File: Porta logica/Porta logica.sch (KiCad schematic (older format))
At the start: 60 parts, among them P1 Input, P2 Batteria, P3 Out, SW1 SW_PUSH, SW2 SW_PUSH, U1 74HC595, U2 LM7805, U3 74HC595, U4 74HC00, U5 74HC595

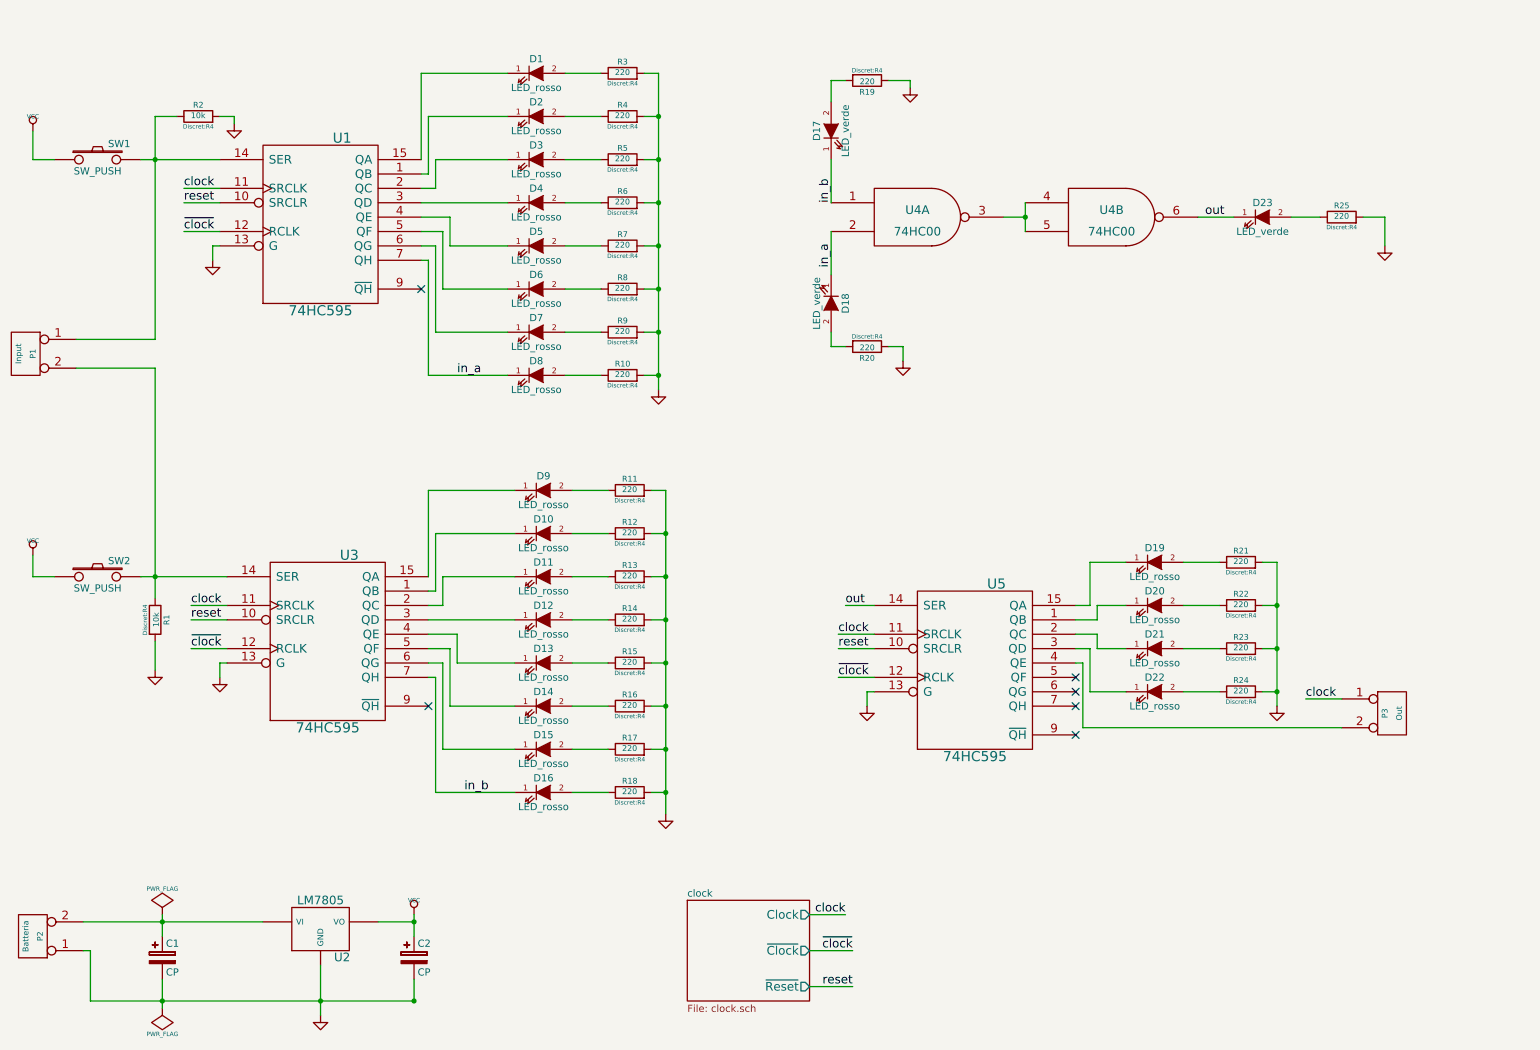
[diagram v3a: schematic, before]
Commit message: Aggiorna footprint resistenze
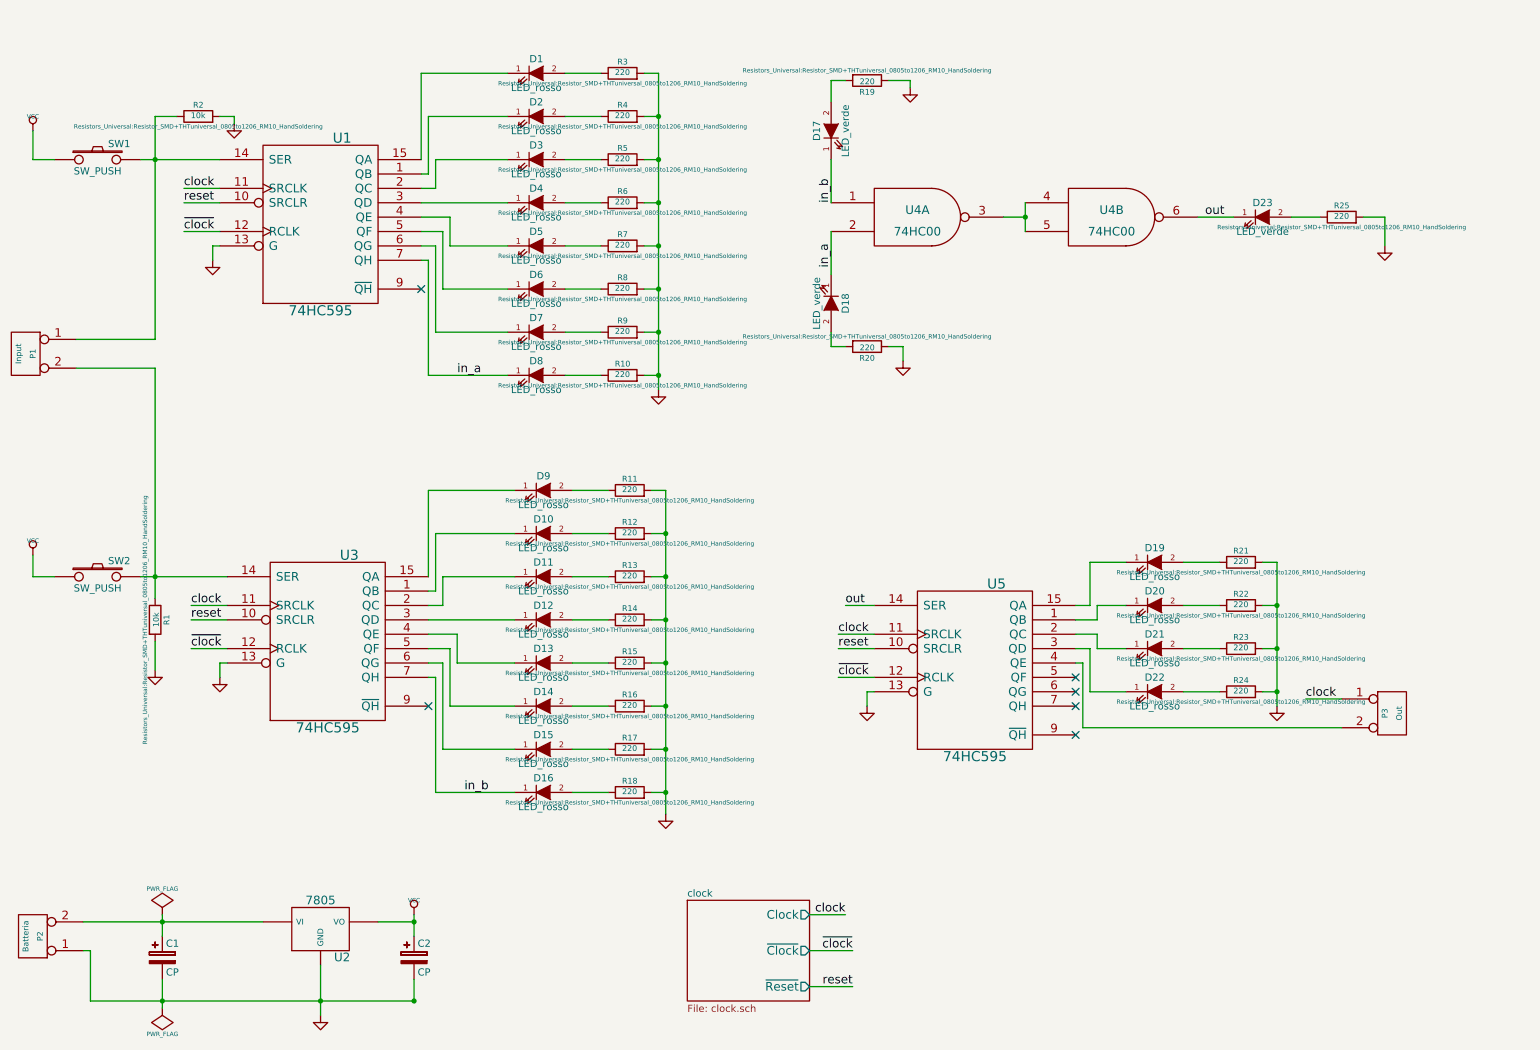
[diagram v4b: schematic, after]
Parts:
- removed U2: LM7805, Housings_SOIC:SOIC-16_7.5x10.3mm_Pitch1.27mm, symbol LM7805
- added U2: 7805, Housings_SOIC:SOIC-16_7.5x10.3mm_Pitch1.27mm, symbol 7805
- R1, R10, R11, R12, R13, R14, R15, R16, R17, R18, R19, R2, R20, R21, R22, R23, R24, R25, R3, R4, R5, R6, R7, R8, R9: footprint Discret:R4 -> Resistors_Universal:Resistor_SMD+THTuniversal_0805to1206_RM10_HandSoldering
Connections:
- net GND: now also U2.GND
- net VCC: now also U2.VO
- net at C1.1, P2.2 (PM): now also U2.VI
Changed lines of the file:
@@
 F 0 "R3" V 4930 1000 40  0000 C CNN
 F 1 "220" V 4857 1001 40  0000 C CNN
-F 2 "Discret:R4" V 4780 1000 30  0000 C CNN
+F 2 "Resistors_Universal:Resistor_SMD+THTuniversal_0805to1206_RM10_HandSoldering" V 4780 1000 30  0000 C CNN
 F 3 "~" H 4850 1000 30  0000 C CNN
 	1    4850 1000
@@
 F 0 "R4" V 4930 1300 40  0000 C CNN
 F 1 "220" V 4857 1301 40  0000 C CNN
-F 2 "Discret:R4" V 4780 1300 30  0000 C CNN
+F 2 "Resistors_Universal:Resistor_SMD+THTuniversal_0805to1206_RM10_HandSoldering" V 4780 1300 30  0000 C CNN
 F 3 "~" H 4850 1300 30  0000 C CNN
 	1    4850 1300
@@
 F 0 "R5" V 4930 1600 40  0000 C CNN
 F 1 "220" V 4857 1601 40  0000 C CNN
-F 2 "Discret:R4" V 4780 1600 30  0000 C CNN
+F 2 "Resistors_Universal:Resistor_SMD+THTuniversal_0805to1206_RM10_HandSoldering" V 4780 1600 30  0000 C CNN
 F 3 "~" H 4850 1600 30  0000 C CNN
 	1    4850 1600
@@
 F 0 "R6" V 4930 1900 40  0000 C CNN
 F 1 "220" V 4857 1901 40  0000 C CNN
-F 2 "Discret:R4" V 4780 1900 30  0000 C CNN
+F 2 "Resistors_Universal:Resistor_SMD+THTuniversal_0805to1206_RM10_HandSoldering" V 4780 1900 30  0000 C CNN
 F 3 "~" H 4850 1900 30  0000 C CNN
 	1    4850 1900
@@
 F 0 "R7" V 4930 2200 40  0000 C CNN
 F 1 "220" V 4857 2201 40  0000 C CNN
-F 2 "Discret:R4" V 4780 2200 30  0000 C CNN
+F 2 "Resistors_Universal:Resistor_SMD+THTuniversal_0805to1206_RM10_HandSoldering" V 4780 2200 30  0000 C CNN
 F 3 "~" H 4850 2200 30  0000 C CNN
 	1    4850 2200
@@
 F 0 "R8" V 4930 2500 40  0000 C CNN
 F 1 "220" V 4857 2501 40  0000 C CNN
-F 2 "Discret:R4" V 4780 2500 30  0000 C CNN
+F 2 "Resistors_Universal:Resistor_SMD+THTuniversal_0805to1206_RM10_HandSoldering" V 4780 2500 30  0000 C CNN
 F 3 "~" H 4850 2500 30  0000 C CNN
 	1    4850 2500
@@
 F 0 "R9" V 4930 2800 40  0000 C CNN
 F 1 "220" V 4857 2801 40  0000 C CNN
-F 2 "Discret:R4" V 4780 2800 30  0000 C CNN
+F 2 "Resistors_Universal:Resistor_SMD+THTuniversal_0805to1206_RM10_HandSoldering" V 4780 2800 30  0000 C CNN
 F 3 "~" H 4850 2800 30  0000 C CNN
 	1    4850 2800
@@
 F 0 "R10" V 4930 3100 40  0000 C CNN
 F 1 "220" V 4857 3101 40  0000 C CNN
-F 2 "Discret:R4" V 4780 3100 30  0000 C CNN
+F 2 "Resistors_Universal:Resistor_SMD+THTuniversal_0805to1206_RM10_HandSoldering" V 4780 3100 30  0000 C CNN
 F 3 "~" H 4850 3100 30  0000 C CNN
 	1    4850 3100
@@
 F 0 "R11" V 4980 3900 40  0000 C CNN
 F 1 "220" V 4907 3901 40  0000 C CNN
-F 2 "Discret:R4" V 4830 3900 30  0000 C CNN
+F 2 "Resistors_Universal:Resistor_SMD+THTuniversal_0805to1206_RM10_HandSoldering" V 4830 3900 30  0000 C CNN
 F 3 "~" H 4900 3900 30  0000 C CNN
 	1    4900 3900
@@
 F 0 "R12" V 4980 4200 40  0000 C CNN
 F 1 "220" V 4907 4201 40  0000 C CNN
-F 2 "Discret:R4" V 4830 4200 30  0000 C CNN
+F 2 "Resistors_Universal:Resistor_SMD+THTuniversal_0805to1206_RM10_HandSoldering" V 4830 4200 30  0000 C CNN
 F 3 "~" H 4900 4200 30  0000 C CNN
 	1    4900 4200
@@
 F 0 "R13" V 4980 4500 40  0000 C CNN
 F 1 "220" V 4907 4501 40  0000 C CNN
-F 2 "Discret:R4" V 4830 4500 30  0000 C CNN
+F 2 "Resistors_Universal:Resistor_SMD+THTuniversal_0805to1206_RM10_HandSoldering" V 4830 4500 30  0000 C CNN
 F 3 "~" H 4900 4500 30  0000 C CNN
 	1    4900 4500
@@
 F 0 "R14" V 4980 4800 40  0000 C CNN
 F 1 "220" V 4907 4801 40  0000 C CNN
-F 2 "Discret:R4" V 4830 4800 30  0000 C CNN
+F 2 "Resistors_Universal:Resistor_SMD+THTuniversal_0805to1206_RM10_HandSoldering" V 4830 4800 30  0000 C CNN
 F 3 "~" H 4900 4800 30  0000 C CNN
 	1    4900 4800
@@
 F 0 "R15" V 4980 5100 40  0000 C CNN
 F 1 "220" V 4907 5101 40  0000 C CNN
-F 2 "Discret:R4" V 4830 5100 30  0000 C CNN
+F 2 "Resistors_Universal:Resistor_SMD+THTuniversal_0805to1206_RM10_HandSoldering" V 4830 5100 30  0000 C CNN
 F 3 "~" H 4900 5100 30  0000 C CNN
 	1    4900 5100
@@
 F 0 "R16" V 4980 5400 40  0000 C CNN
 F 1 "220" V 4907 5401 40  0000 C CNN
-F 2 "Discret:R4" V 4830 5400 30  0000 C CNN
+F 2 "Resistors_Universal:Resistor_SMD+THTuniversal_0805to1206_RM10_HandSoldering" V 4830 5400 30  0000 C CNN
 F 3 "~" H 4900 5400 30  0000 C CNN
 	1    4900 5400
@@
 F 0 "R17" V 4980 5700 40  0000 C CNN
 F 1 "220" V 4907 5701 40  0000 C CNN
-F 2 "Discret:R4" V 4830 5700 30  0000 C CNN
+F 2 "Resistors_Universal:Resistor_SMD+THTuniversal_0805to1206_RM10_HandSoldering" V 4830 5700 30  0000 C CNN
 F 3 "~" H 4900 5700 30  0000 C CNN
 	1    4900 5700
@@
 F 0 "R18" V 4980 6000 40  0000 C CNN
 F 1 "220" V 4907 6001 40  0000 C CNN
-F 2 "Discret:R4" V 4830 6000 30  0000 C CNN
+F 2 "Resistors_Universal:Resistor_SMD+THTuniversal_0805to1206_RM10_HandSoldering" V 4830 6000 30  0000 C CNN
 F 3 "~" H 4900 6000 30  0000 C CNN
 	1    4900 6000
@@
 F 0 "R1" V 1680 4800 40  0000 C CNN
 F 1 "10k" V 1607 4801 40  0000 C CNN
-F 2 "Discret:R4" V 1530 4800 30  0000 C CNN
+F 2 "Resistors_Universal:Resistor_SMD+THTuniversal_0805to1206_RM10_HandSoldering" V 1530 4800 30  0000 C CNN
 F 3 "~" H 1600 4800 30  0000 C CNN
 	1    1600 4800
@@
 F 0 "R2" V 1980 1300 40  0000 C CNN
 F 1 "10k" V 1907 1301 40  0000 C CNN
-F 2 "Discret:R4" V 1830 1300 30  0000 C CNN
+F 2 "Resistors_Universal:Resistor_SMD+THTuniversal_0805to1206_RM10_HandSoldering" V 1830 1300 30  0000 C CNN
 F 3 "~" H 1900 1300 30  0000 C CNN
 	1    1900 1300
@@
 F 0 "R19" V 6630 1050 40  0000 C CNN
 F 1 "220" V 6557 1051 40  0000 C CNN
-F 2 "Discret:R4" V 6480 1050 30  0000 C CNN
+F 2 "Resistors_Universal:Resistor_SMD+THTuniversal_0805to1206_RM10_HandSoldering" V 6480 1050 30  0000 C CNN
 F 3 "~" H 6550 1050 30  0000 C CNN
 	1    6550 1050
@@
 F 0 "R20" V 6630 2900 40  0000 C CNN
 F 1 "220" V 6557 2901 40  0000 C CNN
-F 2 "Discret:R4" V 6480 2900 30  0000 C CNN
+F 2 "Resistors_Universal:Resistor_SMD+THTuniversal_0805to1206_RM10_HandSoldering" V 6480 2900 30  0000 C CNN
 F 3 "~" H 6550 2900 30  0000 C CNN
 	1    6550 2900
@@
 F 0 "R25" V 9930 2000 40  0000 C CNN
 F 1 "220" V 9857 2001 40  0000 C CNN
-F 2 "Discret:R4" V 9780 2000 30  0000 C CNN
+F 2 "Resistors_Universal:Resistor_SMD+THTuniversal_0805to1206_RM10_HandSoldering" V 9780 2000 30  0000 C CNN
 F 3 "~" H 9850 2000 30  0000 C CNN
 	1    9850 2000
@@
 F 0 "R21" V 9230 4400 40  0000 C CNN
 F 1 "220" V 9157 4401 40  0000 C CNN
-F 2 "Discret:R4" V 9080 4400 30  0000 C CNN
+F 2 "Resistors_Universal:Resistor_SMD+THTuniversal_0805to1206_RM10_HandSoldering" V 9080 4400 30  0000 C CNN
 F 3 "~" H 9150 4400 30  0000 C CNN
 	1    9150 4400
@@
 F 0 "R22" V 9230 4700 40  0000 C CNN
 F 1 "220" V 9157 4701 40  0000 C CNN
-F 2 "Discret:R4" V 9080 4700 30  0000 C CNN
+F 2 "Resistors_Universal:Resistor_SMD+THTuniversal_0805to1206_RM10_HandSoldering" V 9080 4700 30  0000 C CNN
 F 3 "~" H 9150 4700 30  0000 C CNN
 	1    9150 4700
@@
 F 0 "R23" V 9230 5000 40  0000 C CNN
 F 1 "220" V 9157 5001 40  0000 C CNN
-F 2 "Discret:R4" V 9080 5000 30  0000 C CNN
+F 2 "Resistors_Universal:Resistor_SMD+THTuniversal_0805to1206_RM10_HandSoldering" V 9080 5000 30  0000 C CNN
 F 3 "~" H 9150 5000 30  0000 C CNN
 	1    9150 5000
@@
 F 0 "R24" V 9230 5300 40  0000 C CNN
 F 1 "220" V 9157 5301 40  0000 C CNN
-F 2 "Discret:R4" V 9080 5300 30  0000 C CNN
+F 2 "Resistors_Universal:Resistor_SMD+THTuniversal_0805to1206_RM10_HandSoldering" V 9080 5300 30  0000 C CNN
 F 3 "~" H 9150 5300 30  0000 C CNN
 	1    9150 5300
@@
 	-1   0    0    1
 $EndComp
-$Comp
-L LM7805 U2
-U 1 1 555F4238
-P 2750 6950
-F 0 "U2" H 2900 6754 60  0000 C CNN
-F 1 "LM7805" H 2750 7150 60  0000 C CNN
-F 2 "Housings_SOIC:SOIC-16_7.5x10.3mm_Pitch1.27mm" H 2750 6950 60  0001 C CNN
-F 3 "" H 2750 6950 60  0000 C CNN
-	1    2750 6950
-	1    0    0    -1
-$EndComp
 Wire Wire Line
 	2750 7200 2750 7550
@@
 Wire Wire Line
 	3150 6900 3400 6900
+$Comp
+L 7805 U2
+U 1 1 555F1A27
+P 2750 6950
+F 0 "U2" H 2900 6754 60  0000 C CNN
+F 1 "7805" H 2750 7150 60  0000 C CNN
+F 2 "Housings_SOIC:SOIC-16_7.5x10.3mm_Pitch1.27mm" H 2750 6950 60  0001 C CNN
+F 3 "" H 2750 6950 60  0000 C CNN
+	1    2750 6950
+	1    0    0    -1
+$EndComp
 $EndSCHEMATC

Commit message: Correggi orientamento LED
I led erano girati al contrario. Togli un led per avere più spazio sulla
scatola esterna.
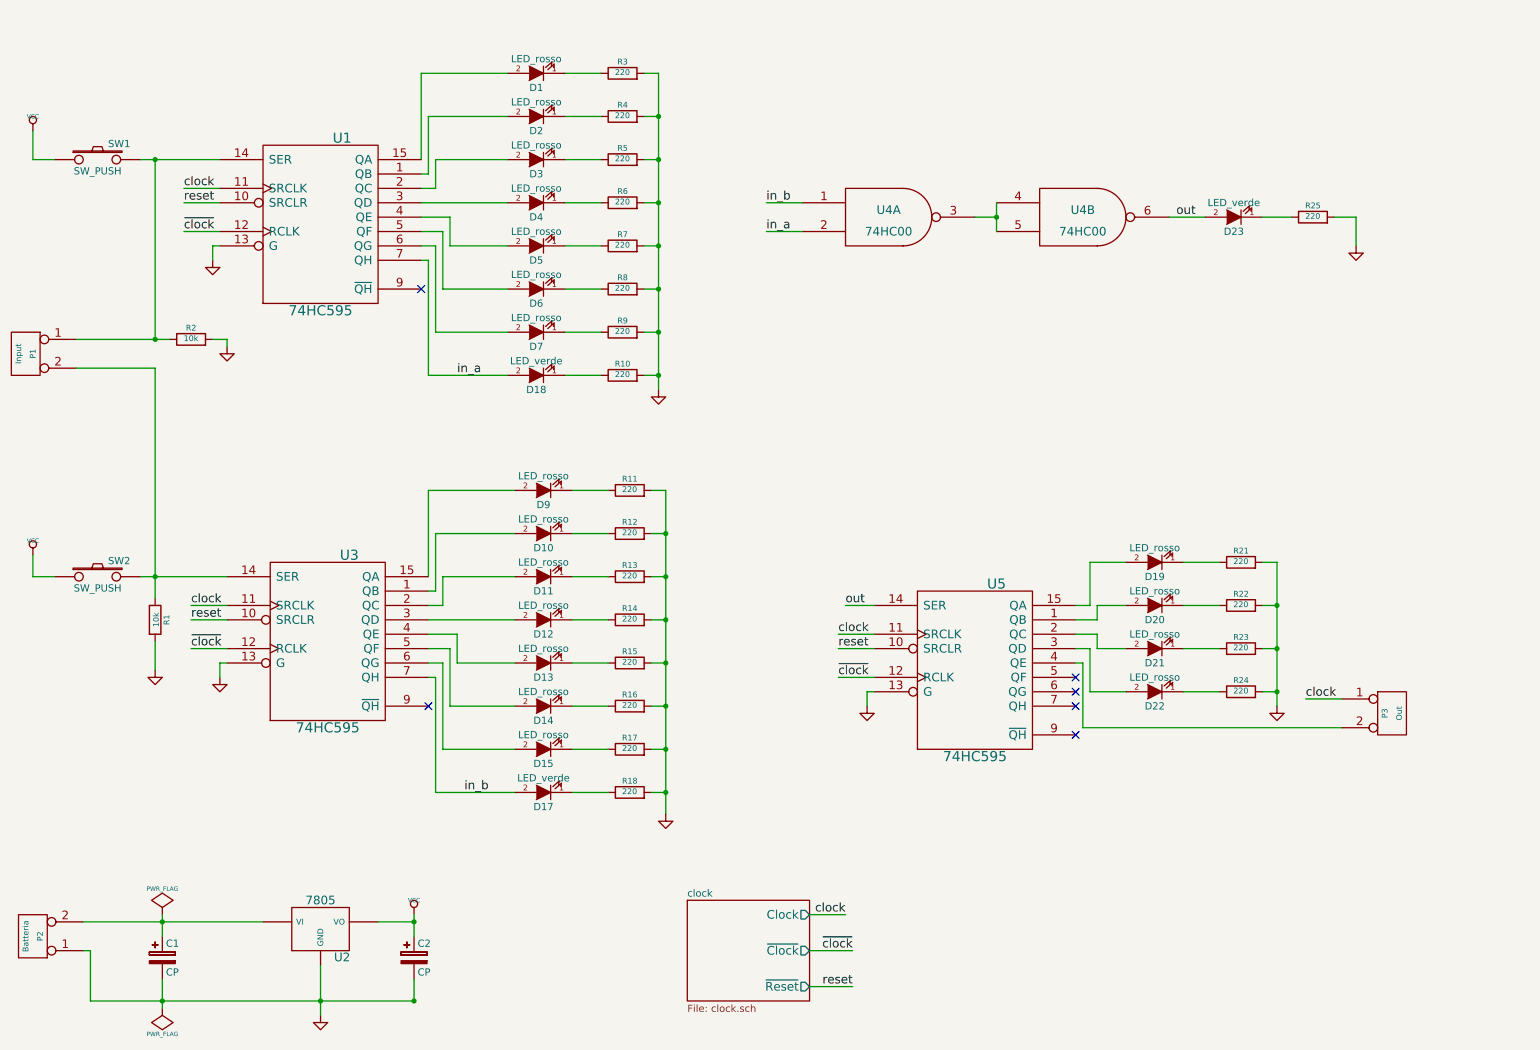
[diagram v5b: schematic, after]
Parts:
- removed D16, D8: LED_rosso, LEDs:LED-5MM, symbol LED
- removed R19, R20: 220, Resistors_Universal:Resistor_SMD+THTuniversal_0805to1206_RM10_HandSoldering, symbol R
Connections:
- net in_a: now also D18.2 (A); no longer D18.1 (K)
- net in_b: now also D17.2 (A); no longer D17.1 (K)
- net out: now also D23.2 (A); no longer D23.1 (K)
- net at U1.1 (QB): now also D2.2 (A); no longer D2.1 (K)
- net at U1.15 (QA): now also D1.2 (A); no longer D1.1 (K)
- net at U1.2 (QC): now also D3.2 (A); no longer D3.1 (K)
- net at U1.3 (QD): now also D4.2 (A); no longer D4.1 (K)
- net at U1.4 (QE): now also D5.2 (A); no longer D5.1 (K)
- net at U1.5 (QF): now also D6.2 (A); no longer D6.1 (K)
- net at U1.6 (QG): now also D7.2 (A); no longer D7.1 (K)
- net at R3.1: now also D1.1 (K); no longer D1.2 (A)
- net at R4.1: now also D2.1 (K); no longer D2.2 (A)
- net at R5.1: now also D3.1 (K); no longer D3.2 (A)
- net at R6.1: now also D4.1 (K); no longer D4.2 (A)
- net at R7.1: now also D5.1 (K); no longer D5.2 (A)
- net at R8.1: now also D6.1 (K); no longer D6.2 (A)
- net at R9.1: now also D7.1 (K); no longer D7.2 (A)
- net at R10.1: now also D18.1 (K)
- net at U3.1 (QB): now also D10.2 (A); no longer D10.1 (K)
- net at U3.15 (QA): now also D9.2 (A); no longer D9.1 (K)
- net at U3.2 (QC): now also D11.2 (A); no longer D11.1 (K)
- net at U3.3 (QD): now also D12.2 (A); no longer D12.1 (K)
- net at U3.4 (QE): now also D13.2 (A); no longer D13.1 (K)
- net at U3.5 (QF): now also D14.2 (A); no longer D14.1 (K)
- net at U3.6 (QG): now also D15.2 (A); no longer D15.1 (K)
- net at R11.1: now also D9.1 (K); no longer D9.2 (A)
- net at R12.1: now also D10.1 (K); no longer D10.2 (A)
- net at R13.1: now also D11.1 (K); no longer D11.2 (A)
- net at R14.1: now also D12.1 (K); no longer D12.2 (A)
- net at R15.1: now also D13.1 (K); no longer D13.2 (A)
- net at R16.1: now also D14.1 (K); no longer D14.2 (A)
- net at R17.1: now also D15.1 (K); no longer D15.2 (A)
- net at R18.1: now also D17.1 (K)
- net at R25.1: now also D23.1 (K); no longer D23.2 (A)
- net at U5.1 (QB): now also D20.2 (A); no longer D20.1 (K)
- net at U5.15 (QA): now also D19.2 (A); no longer D19.1 (K)
- net at U5.2 (QC): now also D21.2 (A); no longer D21.1 (K)
- net at U5.3 (QD): now also D22.2 (A); no longer D22.1 (K)
- net at R21.1: now also D19.1 (K); no longer D19.2 (A)
- net at R22.1: now also D20.1 (K); no longer D20.2 (A)
- net at R23.1: now also D21.1 (K); no longer D21.2 (A)
- net at R24.1: now also D22.1 (K); no longer D22.2 (A)
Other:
- moved on the sheet: D17, D18, D23, R2, R25, U4A, U4B
